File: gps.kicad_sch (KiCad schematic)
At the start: 23 parts, among them J6 SMA, U5 74LVC1G80, U6 ZOE-M8Q, Y1 32.768k

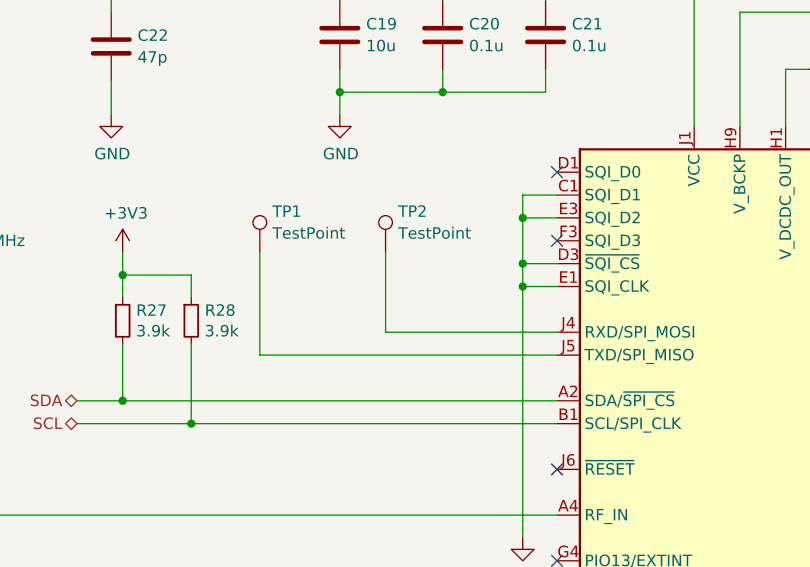
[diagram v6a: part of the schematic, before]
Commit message: fixes from testing, updated for pi5
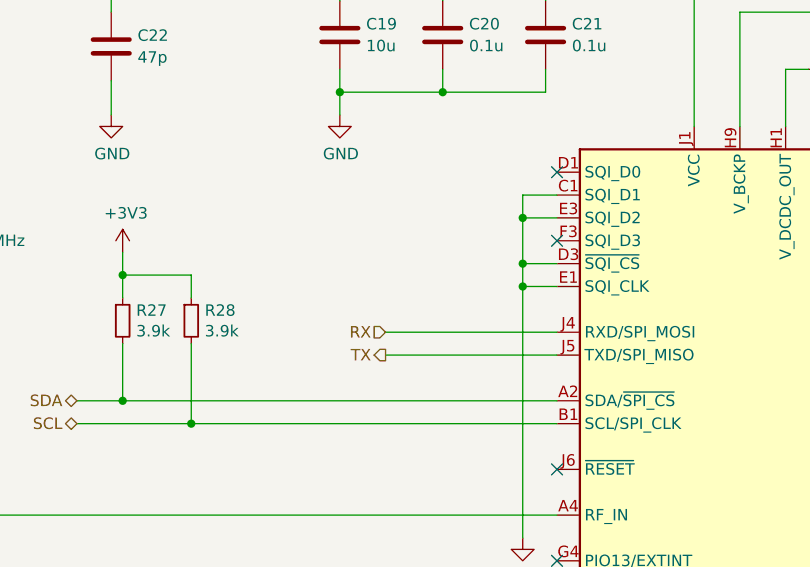
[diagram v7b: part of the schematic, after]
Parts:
- removed TP1, TP2: TestPoint, TestPoint:TestPoint_Pad_1.0x1.0mm, symbol Connector:TestPoint
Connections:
- net RX: now reaches U6.J4 (RXD/SPI_MOSI)
- net TX: now reaches U6.J5 (TXD/SPI_MISO)
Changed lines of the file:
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@@
 	(wire
 		(pts
-			(xy 86.36 91.44) (xy 86.36 80.01)
-		)
-		(stroke
-			(width 0)
-			(type default)
-		)
-	)
-	(wire
-		(pts
 			(xy 95.25 49.53) (xy 106.68 49.53)
 		)
@@
 	(wire
 		(pts
-			(xy 100.33 80.01) (xy 100.33 88.9)
-		)
-		(stroke
-			(width 0)
-			(type default)
-		)
-	)
-	(wire
-		(pts
 			(xy 224.79 78.74) (xy 224.79 73.66)
 		)
@@
 	(wire
 		(pts
-			(xy 119.38 91.44) (xy 86.36 91.44)
+			(xy 119.38 91.44) (xy 100.33 91.44)
 		)
 		(stroke
@@
 		)
 	)
+	(hierarchical_label "TX"
+		(shape output)
+		(at 100.33 91.44 180)
+		(fields_autoplaced yes)
+		(effects
+			(font
+				(size 1.27 1.27)
+			)
+			(justify right)
+		)
+	)
+	(hierarchical_label "RX"
+		(shape input)
+		(at 100.33 88.9 180)
+		(fields_autoplaced yes)
+		(effects
+			(font
+				(size 1.27 1.27)
+			)
+			(justify right)
+		)
+	)
 	(hierarchical_label "SCL"
 		(shape bidirectional)
@@
 	)
 	(symbol
-		(lib_id "Connector:TestPoint")
-		(at 86.36 80.01 0)
-		(unit 1)
-		(exclude_from_sim no)
-		(in_bom yes)
-		(on_board yes)
-		(dnp no)
-		(fields_autoplaced yes)
-		(property "Reference" "TP1"
-			(at 87.757 75.4958 0)
-			(effects
-				(font
-					(size 1.27 1.27)
-				)
-				(justify left)
-			)
-		)
-		(property "Value" "TestPoint"
-			(at 87.757 77.9201 0)
-			(effects
-				(font
-					(size 1.27 1.27)
-				)
-				(justify left)
-			)
-		)
-		(property "Footprint" "TestPoint:TestPoint_Pad_1.0x1.0mm"
-			(at 91.44 80.01 0)
-			(effects
-				(font
-					(size 1.27 1.27)
-				)
-				(hide yes)
-			)
-		)
-		(property "Datasheet" "~"
-			(at 91.44 80.01 0)
-			(effects
-				(font
-					(size 1.27 1.27)
-				)
-				(hide yes)
-			)
-		)
-		(property "Description" "test point"
-			(at 86.36 80.01 0)
-			(effects
-				(font
-					(size 1.27 1.27)
-				)
-				(hide yes)
-			)
-		)
-		(property "Mfg Part Number" "--"
-			(at 86.36 80.01 0)
-			(effects
-				(font
-					(size 1.27 1.27)
-				)
-				(hide yes)
-			)
-		)
-		(pin "1"
-		)
-		(instances
-			(project "dashHat"
-				(path "/e63e39d7-6ac0-4ffd-8aa3-1841a4541b55/490143d4-f9fe-4aeb-b04b-6d8920f8859e"
-					(reference "TP1")
-					(unit 1)
-				)
-			)
-		)
-	)
-	(symbol
 		(lib_id "Device:C")
 		(at 95.25 55.88 0)
@@
 					(unit 1)
 				)
-			)
-		)
-	)
-	(symbol
-		(lib_id "Connector:TestPoint")
-		(at 100.33 80.01 0)
-		(unit 1)
-		(exclude_from_sim no)
-		(in_bom yes)
-		(on_board yes)
-		(dnp no)
-		(fields_autoplaced yes)
-		(property "Reference" "TP2"
-			(at 101.727 75.4958 0)
-			(effects
-				(font
-					(size 1.27 1.27)
-				)
-				(justify left)
-			)
-		)
-		(property "Value" "TestPoint"
-			(at 101.727 77.9201 0)
-			(effects
-				(font
-					(size 1.27 1.27)
-				)
-				(justify left)
-			)
-		)
-		(property "Footprint" "TestPoint:TestPoint_Pad_1.0x1.0mm"
-			(at 105.41 80.01 0)
-			(effects
-				(font
-					(size 1.27 1.27)
-				)
-				(hide yes)
-			)
-		)
-		(property "Datasheet" "~"
-			(at 105.41 80.01 0)
-			(effects
-				(font
-					(size 1.27 1.27)
-				)
-				(hide yes)
-			)
-		)
-		(property "Description" "test point"
-			(at 100.33 80.01 0)
-			(effects
-				(font
-					(size 1.27 1.27)
-				)
-				(hide yes)
-			)
-		)
-		(property "Mfg Part Number" "--"
-			(at 100.33 80.01 0)
-			(effects
-				(font
-					(size 1.27 1.27)
-				)
-				(hide yes)
-			)
-		)
-		(pin "1"
-		)
-		(instances
-			(project "dashHat"
-				(path "/e63e39d7-6ac0-4ffd-8aa3-1841a4541b55/490143d4-f9fe-4aeb-b04b-6d8920f8859e"
-					(reference "TP2")
-					(unit 1)
-				)

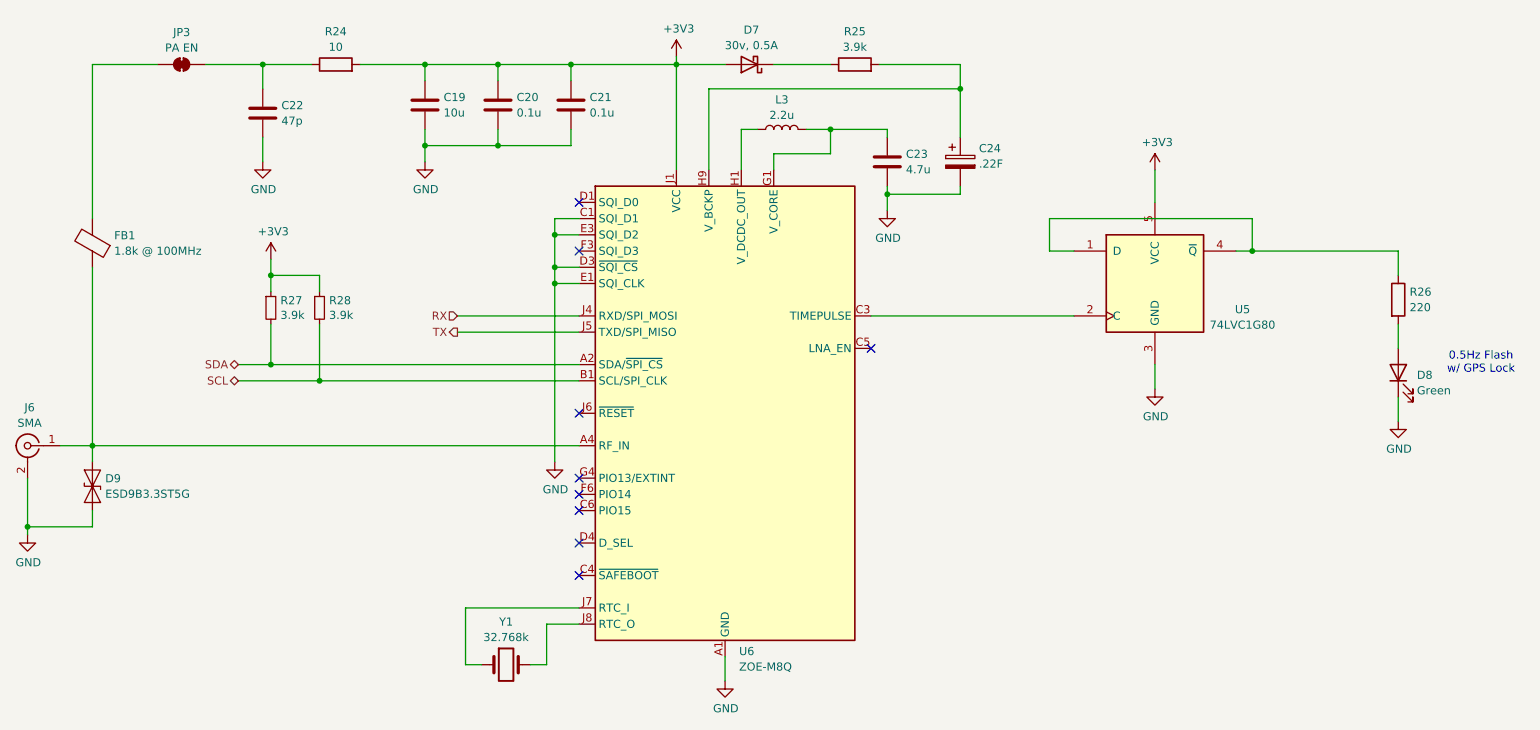
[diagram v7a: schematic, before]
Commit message: update resistors to more commmon values
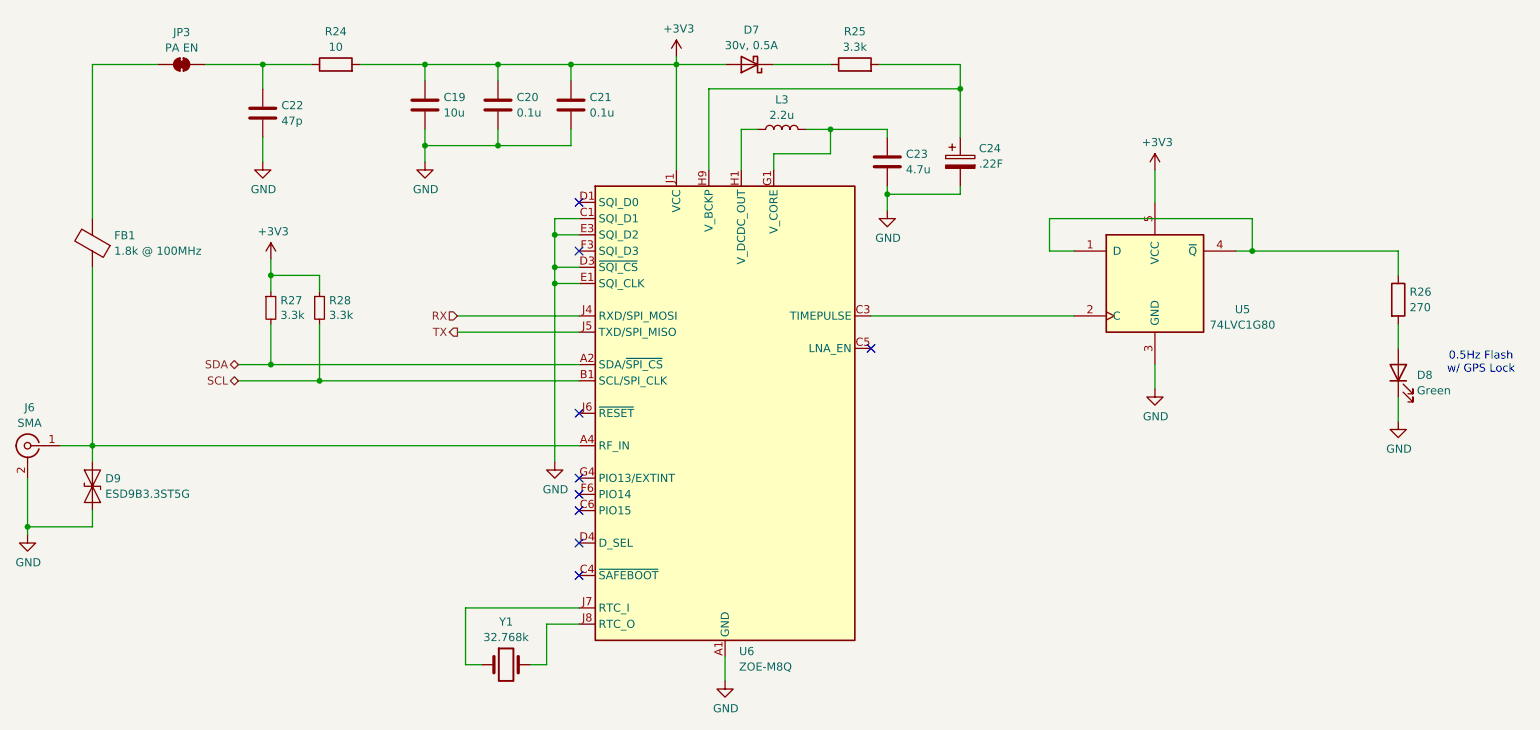
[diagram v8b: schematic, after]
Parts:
- R25, R27, R28: value 3.9k -> 3.3k
- R26: value 220 -> 270
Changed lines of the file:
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@@
 			)
 		)
-		(property "Value" "3.9k"
+		(property "Value" "3.3k"
 			(at 72.6187 88.7793 0)
 			(effects
@@
 			)
 		)
-		(property "Value" "3.9k"
+		(property "Value" "3.3k"
 			(at 80.2387 88.7793 0)
 			(effects
@@
 			)
 		)
-		(property "Value" "220"
+		(property "Value" "270"
 			(at 249.428 87.5721 0)
 			(effects
@@
 			)
 		)
-		(property "Value" "3.9k"
+		(property "Value" "3.3k"
 			(at 162.56 46.7938 90)
 			(effects
